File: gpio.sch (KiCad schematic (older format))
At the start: 38 parts, among them J6 Pro Bus, J7 PMOD1, J8 PMOD, SW1 SW_Push, SW2 SW_Push, U15 TXB0108PWR, U16 TXB0108PWR

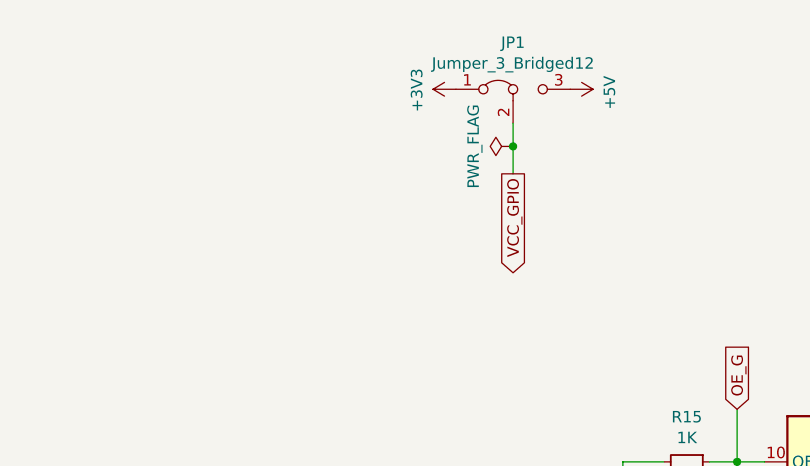
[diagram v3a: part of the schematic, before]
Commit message: consolidated power supply
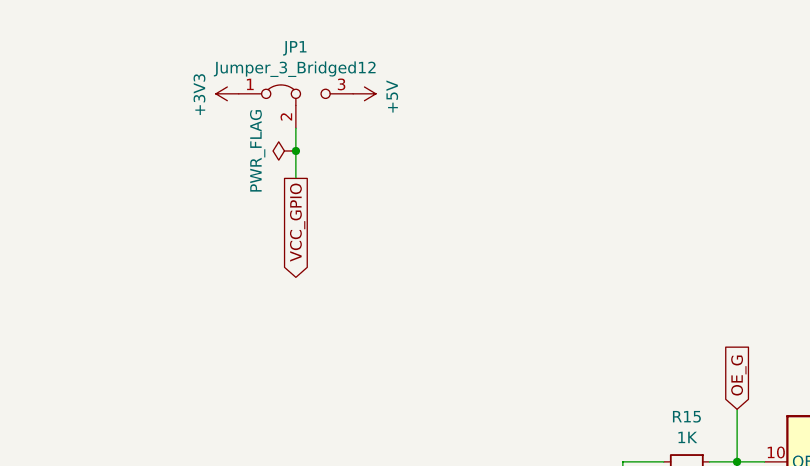
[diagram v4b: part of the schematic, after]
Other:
- moved on the sheet: JP1
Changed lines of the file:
@@
 GPIO_9_F
 Wire Wire Line
-	7140 1180 7140 1280
-Text GLabel 7140 1400 3    50   Output ~ 0
+	6190 1200 6190 1300
+Text GLabel 6190 1420 3    50   Output ~ 0
 VCC_GPIO
 $Comp
 L power:+3V3 #PWR?
 U 1 1 5D04248E
-P 6890 1030
+P 5940 1050
 AR Path="/5CFABACD/5D04248E" Ref="#PWR?"  Part="1"
 AR Path="/5D04248E" Ref="#PWR?"  Part="1"
 AR Path="/5CF9C1ED/5D04248E" Ref="#PWR068"  Part="1"
-F 0 "#PWR068" H 6890 880 50  0001 C CNN
-F 1 "+3V3" H 6790 1200 50  0000 L CNN
-F 2 "" H 6890 1030 50  0001 C CNN
-F 3 "" H 6890 1030 50  0001 C CNN
-	1    6890 1030
+F 0 "#PWR068" H 5940 900 50  0001 C CNN
+F 1 "+3V3" H 5840 1220 50  0000 L CNN
+F 2 "" H 5940 1050 50  0001 C CNN
+F 3 "" H 5940 1050 50  0001 C CNN
+	1    5940 1050
 	0    -1   -1   0
 $EndComp
@@
 L power:+5V #PWR?
 U 1 1 5D042494
-P 7390 1030
+P 6440 1050
 AR Path="/5CFABACD/5D042494" Ref="#PWR?"  Part="1"
 AR Path="/5D042494" Ref="#PWR?"  Part="1"
 AR Path="/5CF9C1ED/5D042494" Ref="#PWR069"  Part="1"
-F 0 "#PWR069" H 7390 880 50  0001 C CNN
-F 1 "+5V" H 7405 1203 50  0000 C CNN
-F 2 "" H 7390 1030 50  0001 C CNN
-F 3 "" H 7390 1030 50  0001 C CNN
-	1    7390 1030
+F 0 "#PWR069" H 6440 900 50  0001 C CNN
+F 1 "+5V" H 6455 1223 50  0000 C CNN
+F 2 "" H 6440 1050 50  0001 C CNN
+F 3 "" H 6440 1050 50  0001 C CNN
+	1    6440 1050
 	0    1    1    0
 $EndComp
@@
 L Jumper:Jumper_3_Bridged12 JP?
 U 1 1 5D04249A
-P 7140 1030
+P 6190 1050
 AR Path="/5D04249A" Ref="JP?"  Part="1"
 AR Path="/5CF9C1ED/5D04249A" Ref="JP1"  Part="1"
-F 0 "JP1" H 7140 1234 50  0000 C CNN
-F 1 "Jumper_3_Bridged12" H 7140 1143 50  0000 C CNN
-F 2 "Connector_PinHeader_2.54mm:PinHeader_1x03_P2.54mm_Vertical" H 7140 1030 50  0001 C CNN
-F 3 "~" H 7140 1030 50  0001 C CNN
-	1    7140 1030
+F 0 "JP1" H 6190 1254 50  0000 C CNN
+F 1 "Jumper_3_Bridged12" H 6190 1163 50  0000 C CNN
+F 2 "Connector_PinHeader_2.54mm:PinHeader_1x03_P2.54mm_Vertical" H 6190 1050 50  0001 C CNN
+F 3 "~" H 6190 1050 50  0001 C CNN
+	1    6190 1050
 	1    0    0    -1
 $EndComp
@@
 L power:PWR_FLAG #FLG03
 U 1 1 5D14DB8F
-P 7140 1280
-F 0 "#FLG03" H 7140 1355 50  0001 C CNN
-F 1 "PWR_FLAG" H 7140 1453 50  0000 C CNN
-F 2 "" H 7140 1280 50  0001 C CNN
-F 3 "~" H 7140 1280 50  0001 C CNN
-	1    7140 1280
+P 6190 1300
+F 0 "#FLG03" H 6190 1375 50  0001 C CNN
+F 1 "PWR_FLAG" H 6190 1473 50  0000 C CNN
+F 2 "" H 6190 1300 50  0001 C CNN
+F 3 "~" H 6190 1300 50  0001 C CNN
+	1    6190 1300
 	0    -1   -1   0
 $EndComp
-Connection ~ 7140 1280
-Wire Wire Line
-	7140 1280 7140 1400
+Connection ~ 6190 1300
+Wire Wire Line
+	6190 1300 6190 1420
 $EndSCHEMATC

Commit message: Updated BOM
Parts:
- C34, C35, C36, C37, C38, C39, C40, C41: MFR KEMET -> Taiyo Yuden; MPN C0805C104K4RACTU -> TMK107BJ104KA-T; SPN 80-C0805C104K4R -> (none)
- D10, D11, D12, D13: MFR (none) -> Littelfuse; MPN (none) -> SP0504BAHTG
- D2, D3, D4, D5, D6, D7, D8, D9: value Blue -> Red; MFR (none) -> Lite-On; MPN (none) -> LTST-C190EKT; SPR (none) -> Mouser
- JP1: footprint Connector_PinHeader_2.54mm:PinHeader_1x03_P2.54mm_Vertical -> Connector_PinHeader_2.54mm:PinHeader_1x03_P2.54mm_Horizontal
- R13, R14: MFR (none) -> Yageo; MPN (none) -> RC0603JR-0710KL; SPR (none) -> Mouser
- R15, R16: MFR (none) -> Yageo; MPN (none) -> RC0603JR-071KL; SPR (none) -> Mouser
- RN10, RN11, RN8, RN9: MFR (none) -> Panasonic; MPN (none) -> EXB-38V221JV; SPR (none) -> Mouser
- RN6, RN7: MFR (none) -> Panasonic; MPN (none) -> EXB-38V271JV; SPR (none) -> Mouser
- SW1, SW2: MFR (none) -> TE Connectivity; MPN (none) -> FSMSM; SPR (none) -> Mouser
- U15, U16: MFR (none) -> Texas Instruments; MPN (none) -> TXB0108PWR; SPR (none) -> Mouser
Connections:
- net +3V3: no longer JP1.1 (A), R13.1, R14.1, RN6.5 (R4.2), RN6.6 (R3.2), RN6.7 (R2.2), RN6.8 (R1.2), RN7.5 (R4.2), RN7.6 (R3.2), RN7.7 (R2.2), RN7.8 (R1.2), U15.2 (VCCA), U16.2 (VCCA)
- net +5V renamed 5V
- new net 3V3: JP1.1 (A), R13.1, R14.1, RN6.5 (R4.2), RN6.6 (R3.2), RN6.7 (R2.2), RN6.8 (R1.2), RN7.5 (R4.2), RN7.6 (R3.2), RN7.7 (R2.2), RN7.8 (R1.2), U15.2 (VCCA), U16.2 (VCCA)
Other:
- moved on the sheet: C36, JP1, R13, SW1

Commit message: updated descriptions and part #'s
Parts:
- C34, C35, C36, C37, C38, C39, C40, C41: Description (none) -> Multilayer Ceramic Capacitors MLCC - SMD/SMT 0.1uF 25V X5R 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; SPN (none) -> 963-TMK107BJ104KA-T; SPURL https://www.mouser.com/ProductDetail/KEMET/C0805C104K4RACTU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 -> https://www.mouser.com/ProductDetail/963-TMK107BJ104KA-T
- D10, D11, D12, D13: Description (none) -> ESD Suppressors / TVS Diodes SP0504BAHTG; SPN (none) -> 576-SP0504BAHTG; SPR (none) -> Mouser; SPURL (none) -> https://www.mouser.com/ProductDetail/576-SP0504BAHTG
- D2, D3, D4, D5, D6, D7, D8, D9: Description (none) -> Standard LEDs - SMD Red Clear 621nm; SPN (none) -> 859-LTST-C190EKT; SPURL (none) -> https://www.mouser.com/ProductDetail/859-LTST-C190EKT
- R13, R14: Description (none) -> Thick Film Resistors - SMD 10K OHM 5%; SPN (none) -> 603-RC0603JR-0710KL; SPURL (none) -> https://www.mouser.com/ProductDetail/603-RC0603JR-0710KL
- R15, R16: Description (none) -> Thick Film Resistors - SMD 1K OHM 5%; SPN (none) -> 603-RC0603JR-071KL; SPURL (none) -> https://www.mouser.com/ProductDetail/603-RC0603JR-071KL
- RN10, RN11, RN8, RN9: Description (none) -> Resistor Networks & Arrays 220 OHM 5%; SPN (none) -> 667-EXB-38V221JV; SPURL (none) -> https://www.mouser.com/ProductDetail/667-EXB-38V221JV
- RN6, RN7: Description (none) -> Resistor Networks & Arrays Resistor Array Chip 4 elements; SPN (none) -> 667-EXB-38V271JV; SPURL (none) -> https://www.mouser.com/ProductDetail/667-EXB-38V271JV
- SW1, SW2: Description (none) -> Tactile Switches 3.5X6 SMT TACT TACT SWITCH; SPN (none) -> 506-FSMSM; SPURL (none) -> https://www.mouser.com/ProductDetail/506-FSMSM
- U15, U16: Description (none) -> Translation - Voltage Levels 8-Bit Bi-directional V-Level T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; SPN (none) -> 595-TXB0108PWR; SPURL (none) -> https://www.mouser.com/ProductDetail/595-TXB0108PWR

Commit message: added clock controller/programmer
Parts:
- JP1: footprint Connector_PinHeader_2.54mm:PinHeader_1x03_P2.54mm_Horizontal -> Connector_PinHeader_2.54mm:PinHeader_1x03_P2.54mm_Vertical
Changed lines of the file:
@@
 F 0 "JP1" H 6090 1904 50  0000 C CNN
 F 1 "Jumper_3_Bridged12" H 6090 1813 50  0000 C CNN
-F 2 "Connector_PinHeader_2.54mm:PinHeader_1x03_P2.54mm_Horizontal" H 6090 1700 50  0001 C CNN
+F 2 "Connector_PinHeader_2.54mm:PinHeader_1x03_P2.54mm_Vertical" H 6090 1700 50  0001 C CNN
 F 3 "~" H 6090 1700 50  0001 C CNN
 	1    6090 1700

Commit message: mirror flipped the chips
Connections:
- net GPIO_13: now also U16.12 (B8); no longer U16.15 (B5)
- net GPIO_13_F: now also U16.9 (A8); no longer U16.6 (A5)
- net GPIO_14: now also U16.13 (B7); no longer U16.14 (B6)
- net GPIO_14_F: now also U16.8 (A7); no longer U16.7 (A6)
- net GPIO_15: now also U16.14 (B6); no longer U16.13 (B7)
- net GPIO_15_F: now also U16.7 (A6); no longer U16.8 (A7)
- net GPIO_16: now also U16.15 (B5); no longer U16.12 (B8)
- net GPIO_16_F: now also U16.6 (A5); no longer U16.9 (A8)
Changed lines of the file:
@@
 Text GLabel 9040 2760 2    50   3State ~ 0
 GPIO_1
-Text GLabel 9040 5640 2    50   3State ~ 0
-GPIO_16
-Text GLabel 9040 5540 2    50   3State ~ 0
-GPIO_15
-Text GLabel 9040 5440 2    50   3State ~ 0
-GPIO_14
-Text GLabel 9040 5340 2    50   3State ~ 0
-GPIO_13
 Text GLabel 9040 5240 2    50   3State ~ 0
 GPIO_12
@@
 GPIO_1_F
 Text GLabel 8240 5640 0    50   3State ~ 0
-GPIO_16_F
-Text GLabel 8240 5540 0    50   3State ~ 0
-GPIO_15_F
-Text GLabel 8240 5440 0    50   3State ~ 0
-GPIO_14_F
-Text GLabel 8240 5340 0    50   3State ~ 0
 GPIO_13_F
 Text GLabel 8240 5240 0    50   3State ~ 0
@@
 Connection ~ 3230 1530
 Connection ~ 6090 1950
+Text GLabel 9040 5640 2    50   3State ~ 0
+GPIO_13
+Text GLabel 9040 5540 2    50   3State ~ 0
+GPIO_14
+Text GLabel 9040 5440 2    50   3State ~ 0
+GPIO_15
+Text GLabel 9040 5340 2    50   3State ~ 0
+GPIO_16
+Text GLabel 8240 5540 0    50   3State ~ 0
+GPIO_14_F
+Text GLabel 8240 5440 0    50   3State ~ 0
+GPIO_15_F
+Text GLabel 8240 5340 0    50   3State ~ 0
+GPIO_16_F
 $EndSCHEMATC
